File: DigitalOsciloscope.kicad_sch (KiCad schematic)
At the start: 0 parts

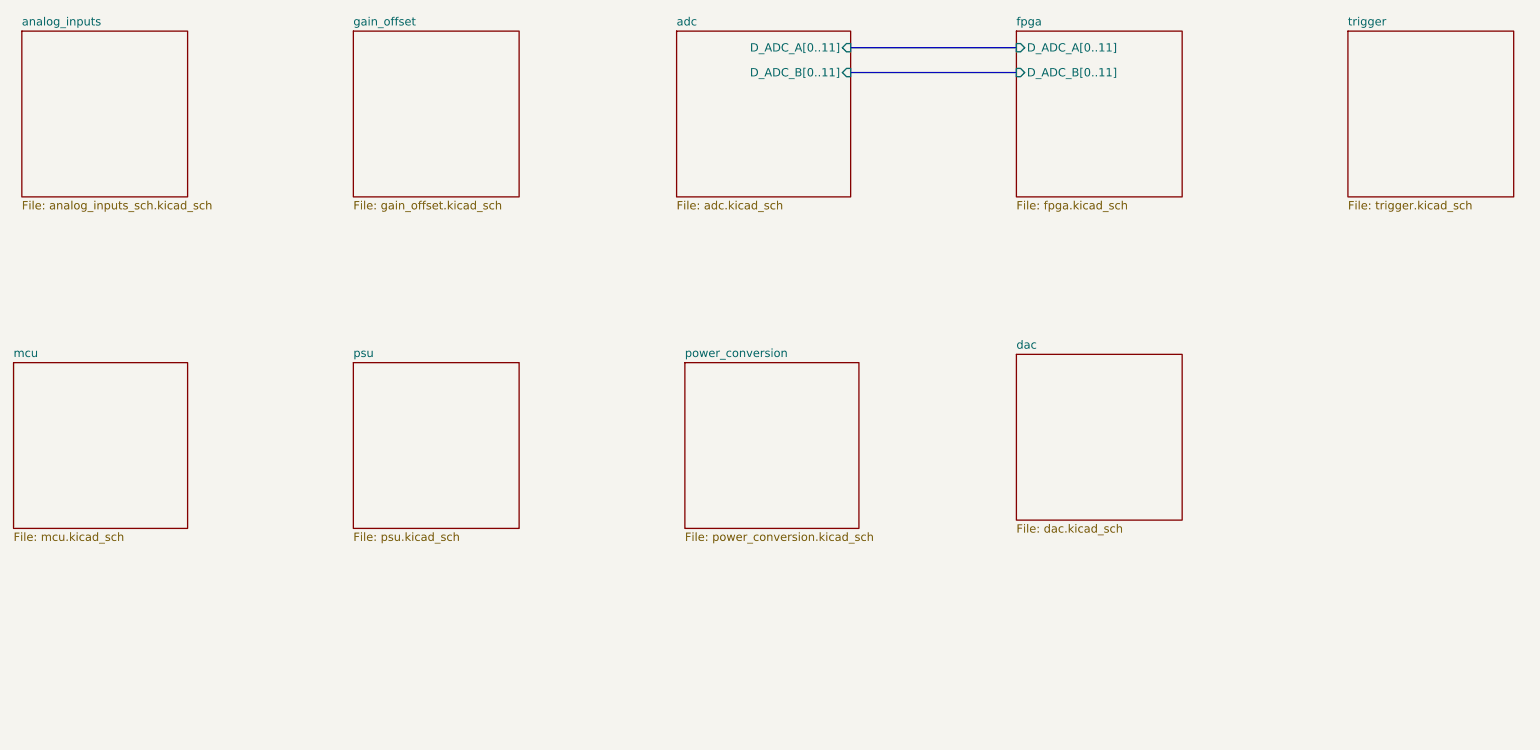
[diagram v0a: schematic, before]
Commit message: Simplifying the design
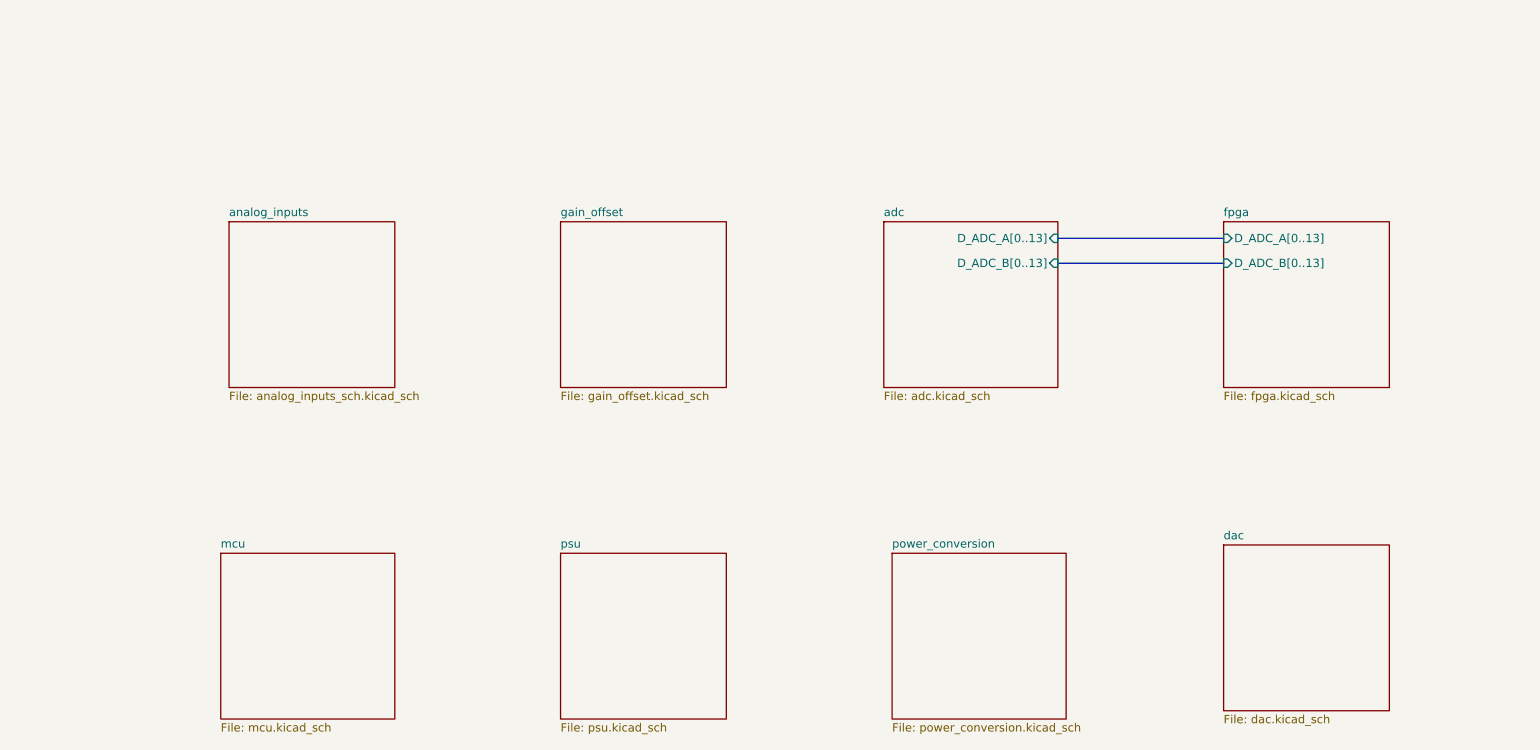
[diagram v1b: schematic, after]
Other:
- removed sheet trigger
- sheet adc ports: added D_ADC_A[0..13], D_ADC_B[0..13]; removed D_ADC_A[0..11], D_ADC_B[0..11]
- sheet fpga ports: added D_ADC_A[0..13], D_ADC_B[0..13]; removed D_ADC_A[0..11], D_ADC_B[0..11]
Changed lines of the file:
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@@
 	(bus
 		(pts
-			(xy 152.4 31.75) (xy 177.8 31.75)
+			(xy 184.15 60.96) (xy 209.55 60.96)
 		)
 		(stroke
@@
 	(bus
 		(pts
-			(xy 152.4 27.94) (xy 177.8 27.94)
+			(xy 184.15 57.15) (xy 209.55 57.15)
 		)
 		(stroke
@@
 	)
 	(sheet
-		(at 177.8 25.4)
+		(at 209.55 54.61)
 		(size 25.4 25.4)
 		(exclude_from_sim no)
@@
 		)
 		(property "Sheetname" "fpga"
-			(at 177.8 24.6884 0)
+			(at 209.55 53.8984 0)
 			(effects
 				(font
@@
 		)
 		(property "Sheetfile" "fpga.kicad_sch"
-			(at 177.8 51.3846 0)
-			(effects
-				(font
-					(size 1.27 1.27)
-				)
-				(justify left top)
-			)
-		)
-		(pin "D_ADC_A[0..11]" input
-			(at 177.8 27.94 180)
+			(at 209.55 80.5946 0)
+			(effects
+				(font
+					(size 1.27 1.27)
+				)
+				(justify left top)
+			)
+		)
+		(pin "D_ADC_A[0..13]" input
+			(at 209.55 57.15 180)
 			(effects
 				(font
@@
 			)
 		)
-		(pin "D_ADC_B[0..11]" input
-			(at 177.8 31.75 180)
+		(pin "D_ADC_B[0..13]" input
+			(at 209.55 60.96 180)
 			(effects
 				(font
@@
 			(project "DigitalOsciloscope"
 				(path "/553deb7b-4100-40fe-99d2-0c7b4b56aad2"
-					(page "9")
-				)
-			)
-		)
-	)
-	(sheet
-		(at 76.2 76.2)
+					(page "5")
+				)
+			)
+		)
+	)
+	(sheet
+		(at 107.95 105.41)
 		(size 25.4 25.4)
 		(exclude_from_sim no)
@@
 		)
 		(property "Sheetname" "psu"
-			(at 76.2 75.4884 0)
+			(at 107.95 104.6984 0)
 			(effects
 				(font
@@
 		)
 		(property "Sheetfile" "psu.kicad_sch"
-			(at 76.2 102.1846 0)
+			(at 107.95 131.3946 0)
 			(effects
 				(font
@@
 	)
 	(sheet
-		(at 24.13 76.2)
+		(at 55.88 105.41)
 		(size 26.67 25.4)
 		(exclude_from_sim no)
@@
 		)
 		(property "Sheetname" "mcu"
-			(at 24.13 75.4884 0)
+			(at 55.88 104.6984 0)
 			(effects
 				(font
@@
 		)
 		(property "Sheetfile" "mcu.kicad_sch"
-			(at 24.13 102.1846 0)
+			(at 55.88 131.3946 0)
 			(effects
 				(font
@@
 	)
 	(sheet
-		(at 177.8 74.93)
+		(at 209.55 104.14)
 		(size 25.4 25.4)
 		(exclude_from_sim no)
@@
 		)
 		(property "Sheetname" "dac"
-			(at 177.8 74.2184 0)
+			(at 209.55 103.4284 0)
 			(effects
 				(font
@@
 		)
 		(property "Sheetfile" "dac.kicad_sch"
-			(at 177.8 100.9146 0)
+			(at 209.55 130.1246 0)
 			(effects
 				(font
@@
 	)
 	(sheet
-		(at 127 76.2)
+		(at 158.75 105.41)
 		(size 26.67 25.4)
 		(exclude_from_sim no)
@@
 		)
 		(property "Sheetname" "power_conversion"
-			(at 127 75.4884 0)
+			(at 158.75 104.6984 0)
 			(effects
 				(font
@@
 		)
 		(property "Sheetfile" "power_conversion.kicad_sch"
-			(at 127 102.1846 0)
+			(at 158.75 131.3946 0)
 			(effects
 				(font
@@
 	)
 	(sheet
-		(at 125.73 25.4)
+		(at 157.48 54.61)
 		(size 26.67 25.4)
 		(exclude_from_sim no)
@@
 		)
 		(property "Sheetname" "adc"
-			(at 125.73 24.6884 0)
+			(at 157.48 53.8984 0)
 			(effects
 				(font
@@
 		)
 		(property "Sheetfile" "adc.kicad_sch"
-			(at 125.73 51.3846 0)
-			(effects
-				(font
-					(size 1.27 1.27)
-				)
-				(justify left top)
-			)
-		)
-		(pin "D_ADC_A[0..11]" input
-			(at 152.4 27.94 0)
+			(at 157.48 80.5946 0)
+			(effects
+				(font
+					(size 1.27 1.27)
+				)
+				(justify left top)
+			)
+		)
+		(pin "D_ADC_A[0..13]" input
+			(at 184.15 57.15 0)
 			(effects
 				(font
@@
 			)
 		)
-		(pin "D_ADC_B[0..11]" input
-			(at 152.4 31.75 0)
+		(pin "D_ADC_B[0..13]" input
+			(at 184.15 60.96 0)
 			(effects
 				(font
@@
 	)
 	(sheet
-		(at 228.6 25.4)
-		(size 25.4 25.4)
-		(exclude_from_sim no)
-		(in_bom yes)
-		(on_board yes)
-		(dnp no)
-		(fields_autoplaced yes)
-		(stroke
-			(width 0.1524)
-			(type solid)
-		)
-		(fill
-			(color 0 0 0 0.0000)
-		)
-		(property "Sheetname" "trigger"
-			(at 228.6 24.6884 0)
-			(effects
-				(font
-					(size 1.27 1.27)
-				)
-				(justify left bottom)
-			)
-		)
-		(property "Sheetfile" "trigger.kicad_sch"
-			(at 228.6 51.3846 0)
-			(effects
-				(font
-					(size 1.27 1.27)
-				)
-				(justify left top)
-			)
-		)
-		(instances
-			(project "DigitalOsciloscope"
-				(path "/553deb7b-4100-40fe-99d2-0c7b4b56aad2"
-					(page "5")
-				)
-			)
-		)
-	)
-	(sheet
-		(at 76.2 25.4)
+		(at 107.95 54.61)
 		(size 25.4 25.4)
 		(exclude_from_sim no)
@@
 		)
 		(property "Sheetname" "gain_offset"
-			(at 76.2 24.6884 0)
+			(at 107.95 53.8984 0)
 			(effects
 				(font
@@
 		)
 		(property "Sheetfile" "gain_offset.kicad_sch"
-			(at 76.2 51.3846 0)
+			(at 107.95 80.5946 0)
 			(effects
 				(font
@@
 	)
 	(sheet
-		(at 25.4 25.4)
+		(at 57.15 54.61)
 		(size 25.4 25.4)
 		(exclude_from_sim no)
@@
 		)
 		(property "Sheetname" "analog_inputs"
-			(at 25.4 24.6884 0)
+			(at 57.15 53.8984 0)
 			(effects
 				(font
@@
 		)
 		(property "Sheetfile" "analog_inputs_sch.kicad_sch"
-			(at 25.4 51.3846 0)
-			(effects
-				(font
+			(at 57.15 80.5946 0)
+			(effects
+				(font

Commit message: Finished schematic?
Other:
- removed sheet power_conversion
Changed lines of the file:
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@@
 	)
 	(sheet
-		(at 209.55 104.14)
+		(at 158.75 105.41)
 		(size 25.4 25.4)
 		(exclude_from_sim no)
@@
 		)
 		(property "Sheetname" "dac"
-			(at 209.55 103.4284 0)
+			(at 158.75 104.6984 0)
 			(effects
 				(font
@@
 		)
 		(property "Sheetfile" "dac.kicad_sch"
-			(at 209.55 130.1246 0)
+			(at 158.75 131.3946 0)
 			(effects
 				(font
@@
 				)
 			)
-		)
-	)
-	(sheet
-		(at 158.75 105.41)
-		(size 26.67 25.4)
-		(exclude_from_sim no)
-		(in_bom yes)
-		(on_board yes)
-		(dnp no)
-		(fields_autoplaced yes)
-		(stroke
-			(width 0.1524)
-			(type solid)
-		)
-		(fill
-			(color 0 0 0 0.0000)
-		)
-		(property "Sheetname" "power_conversion"
-			(at 158.75 104.6984 0)
-			(effects
-				(font
-					(size 1.27 1.27)
-				)
-				(justify left bottom)
-			)
-		)
-		(property "Sheetfile" "power_conversion.kicad_sch"
-			(at 158.75 131.3946 0)
-			(effects
-				(font
-					(size 1.27 1.27)
-				)
-				(justify left top)
-			)
-		)
-		(instances
-			(project "DigitalOsciloscope"
-				(path "/553deb7b-4100-40fe-99d2-0c7b4b56aad2"
-					(page "11")
-				)
-			)

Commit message: Almost finishing schematic
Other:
- removed sheet gain_offset
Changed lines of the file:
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@@
 	(bus
 		(pts
-			(xy 184.15 60.96) (xy 209.55 60.96)
+			(xy 134.62 62.23) (xy 160.02 62.23)
 		)
 		(stroke
@@
 	(bus
 		(pts
-			(xy 184.15 57.15) (xy 209.55 57.15)
+			(xy 134.62 58.42) (xy 160.02 58.42)
 		)
 		(stroke
@@
 	)
 	(sheet
-		(at 209.55 54.61)
+		(at 160.02 55.88)
 		(size 25.4 25.4)
 		(exclude_from_sim no)
@@
 		)
 		(property "Sheetname" "fpga"
-			(at 209.55 53.8984 0)
+			(at 160.02 55.1684 0)
 			(effects
 				(font
@@
 		)
 		(property "Sheetfile" "fpga.kicad_sch"
-			(at 209.55 80.5946 0)
+			(at 160.02 81.8646 0)
 			(effects
 				(font
@@
 		)
 		(pin "D_ADC_A[0..13]" input
-			(at 209.55 57.15 180)
+			(at 160.02 58.42 180)
 			(effects
 				(font
@@
 		)
 		(pin "D_ADC_B[0..13]" input
-			(at 209.55 60.96 180)
+			(at 160.02 62.23 180)
 			(effects
 				(font
@@
 	)
 	(sheet
-		(at 157.48 54.61)
+		(at 107.95 55.88)
 		(size 26.67 25.4)
 		(exclude_from_sim no)
@@
 		)
 		(property "Sheetname" "adc"
-			(at 157.48 53.8984 0)
+			(at 107.95 55.1684 0)
 			(effects
 				(font
@@
 		)
 		(property "Sheetfile" "adc.kicad_sch"
-			(at 157.48 80.5946 0)
+			(at 107.95 81.8646 0)
 			(effects
 				(font
@@
 		)
 		(pin "D_ADC_A[0..13]" input
-			(at 184.15 57.15 0)
+			(at 134.62 58.42 0)
 			(effects
 				(font
@@
 		)
 		(pin "D_ADC_B[0..13]" input
-			(at 184.15 60.96 0)
+			(at 134.62 62.23 0)
 			(effects
 				(font
@@
 				)
 			)
-		)
-	)
-	(sheet
-		(at 107.95 54.61)
-		(size 25.4 25.4)
-		(exclude_from_sim no)
-		(in_bom yes)
-		(on_board yes)
-		(dnp no)
-		(fields_autoplaced yes)
-		(stroke
-			(width 0.1524)
-			(type solid)
-		)
-		(fill
-			(color 0 0 0 0.0000)
-		)
-		(property "Sheetname" "gain_offset"
-			(at 107.95 53.8984 0)
-			(effects
-				(font
-					(size 1.27 1.27)
-				)
-				(justify left bottom)
-			)
-		)
-		(property "Sheetfile" "gain_offset.kicad_sch"
-			(at 107.95 80.5946 0)
-			(effects
-				(font
-					(size 1.27 1.27)
-				)
-				(justify left top)
-			)
-		)
-		(instances
-			(project "DigitalOsciloscope"
-				(path "/553deb7b-4100-40fe-99d2-0c7b4b56aad2"
-					(page "3")
-				)
-			)
